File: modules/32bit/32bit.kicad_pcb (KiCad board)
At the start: 2 copper layers, 30.5 x 68.6 mm, 17 parts, among them J5 USB_C_Receptacle_USB2.0_14P, SW1 K2-1808SN-A4SW-01, SW2 K2-1808SN-A4SW-01, U1 ESP32-S3-WROOM-1U-N16R8

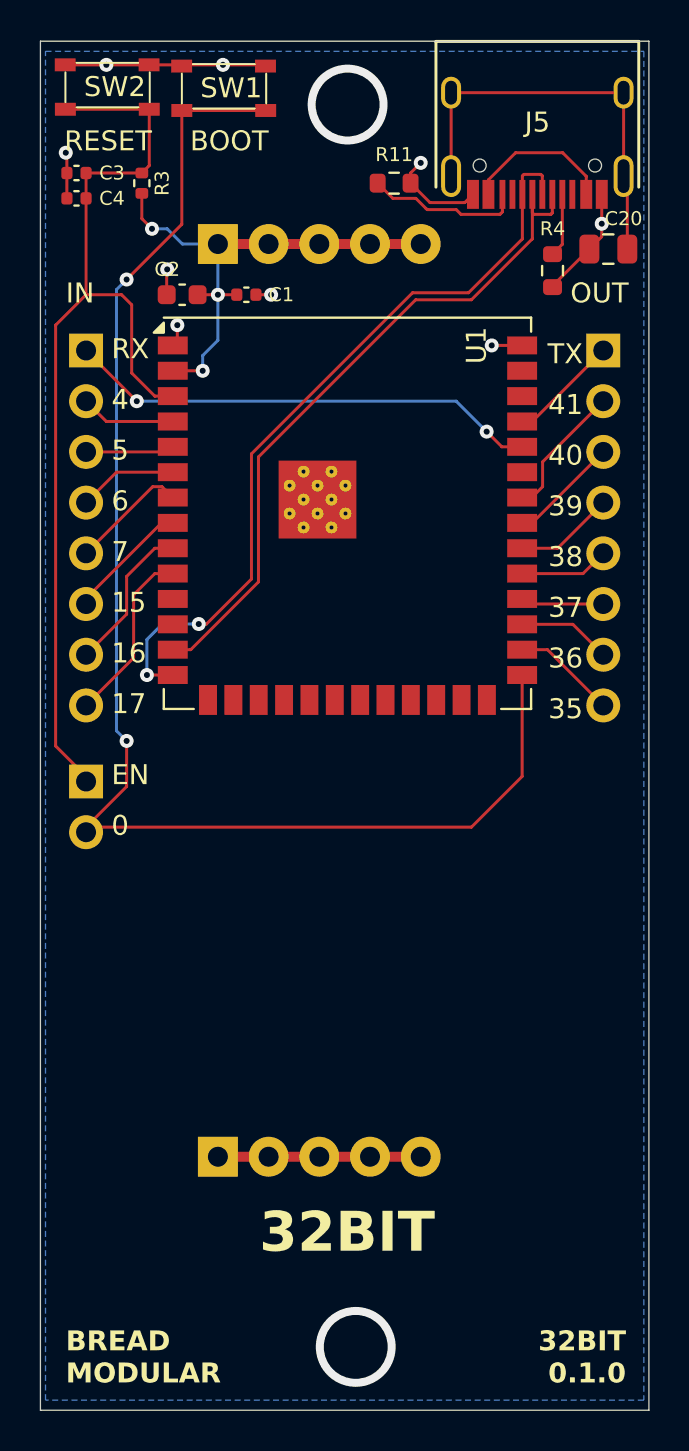
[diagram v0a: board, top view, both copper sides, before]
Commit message: Add 32bit schematics
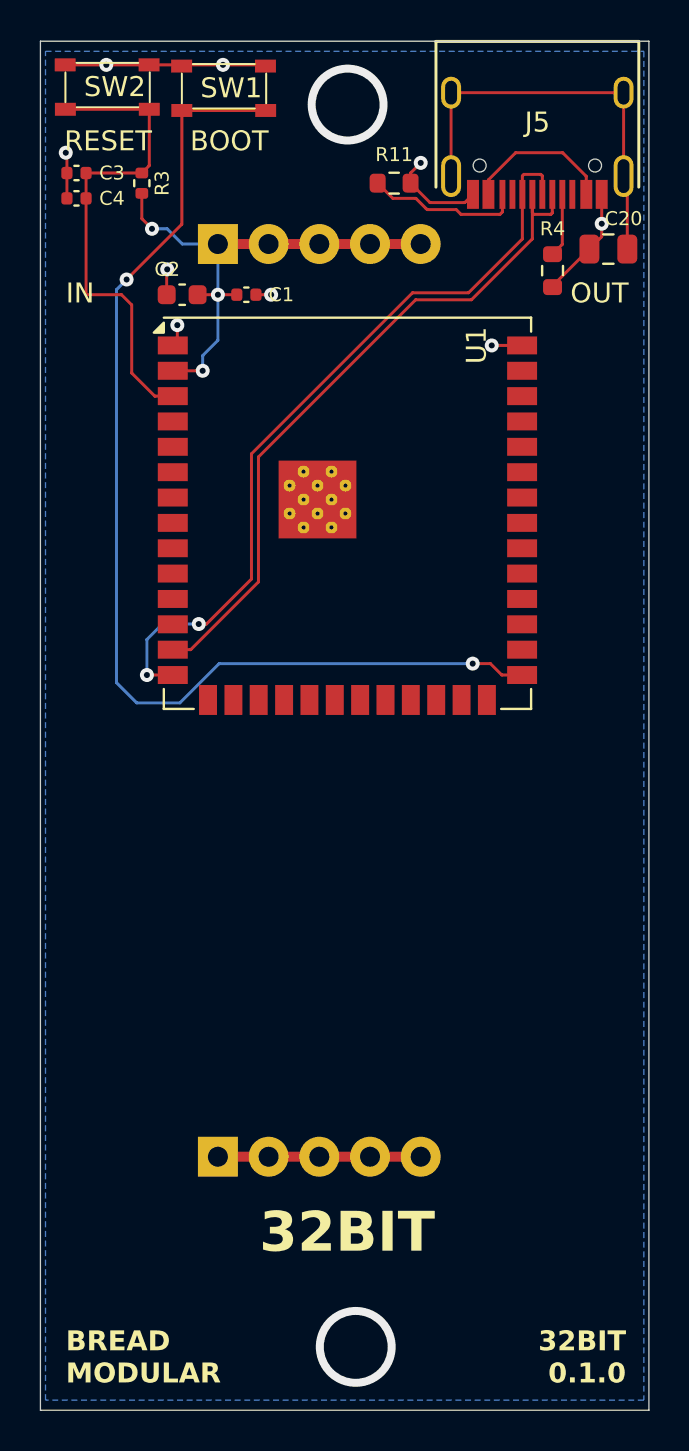
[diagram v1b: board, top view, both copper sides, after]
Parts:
- removed INPUT1, OUTPUT1: Conn_01x08_Socket, Connector_PinSocket_2.54mm:PinSocket_1x08_P2.54mm_Vertical
- removed INPUT2: Conn_01x02_Socket, Connector_PinSocket_2.54mm:PinSocket_1x02_P2.54mm_Vertical
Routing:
- net EN: track 50.3 -> 24.9 mm
- net RX: track 23.8 -> 0.00 mm, vias 2 -> 0
- net IO0: track 70.5 -> 56.0 mm
- net IO17: track 8.93 -> 0.00 mm
- net IO16: track 7.66 -> 0.00 mm
- net IO41: track 6.79 -> 0.00 mm
- net IO15: track 6.19 -> 0.00 mm
- net IO7: track 5.95 -> 0.00 mm
- net TX: track 5.54 -> 0.00 mm
- net IO40: track 5.54 -> 0.00 mm
- net IO35: track 5.22 -> 0.00 mm
- net IO39: track 5.01 -> 0.00 mm
- net IO6: track 4.98 -> 0.00 mm
- net IO4: track 4.76 -> 0.00 mm
- net IO36: track 4.70 -> 0.00 mm
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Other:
- board text removed: "0"
- board text removed: "15"
- board text removed: "16"
- board text removed: "17"
- board text removed: "35"
- board text removed: "36"
- board text removed: "37"
- board text removed: "38"
- board text removed: "39"
- board text removed: "4"
- board text removed: "40"
- board text removed: "41"
- board text removed: "5"
- board text removed: "6"
- board text removed: "7"
- board text removed: "EN"
- board text removed: "RX"
- board text removed: "TX"

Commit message: Finished basic routing
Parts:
- added C21: 0.1uf, Capacitor_SMD:C_0402_1005Metric, F.Cu at (67.3, 78.5)
- added C22: 0.1uf, Capacitor_SMD:C_0402_1005Metric, F.Cu at (65.8, 80.0)
- added C26: 0.1uf, Capacitor_SMD:C_0402_1005Metric, F.Cu at (73.4, 84.3)
- added C27: 10uf, Capacitor_SMD:C_0402_1005Metric, F.Cu at (64.8, 83.8)
- added C33: 10uf, Capacitor_SMD:C_0402_1005Metric, F.Cu at (73.4, 78.7)
- added C34: 0.1uf, Capacitor_SMD:C_0402_1005Metric, F.Cu at (73.4, 79.8)
- added C35: 10uf, Capacitor_SMD:C_0402_1005Metric, F.Cu at (73.4, 81.0)
- added C36: 0.1uf, Capacitor_SMD:C_0402_1005Metric, F.Cu at (73.3, 82.0)
- added C37: 10uf, Capacitor_SMD:C_0402_1005Metric, F.Cu at (73.4, 83.3)
- added C38: 10uf, Capacitor_SMD:C_0402_1005Metric, F.Cu at (73.3, 86.6)
- added C39: 0.1uf, Capacitor_SMD:C_0402_1005Metric, F.Cu at (73.4, 85.6)
- added C5: 10uf, Capacitor_SMD:C_0402_1005Metric, F.Cu at (66.3, 78.5)
- added C6: 0.1uf, Capacitor_SMD:C_0402_1005Metric, F.Cu at (54.9, 82.3)
- added D1: LED, LED_SMD:LED_0603_1608Metric, F.Cu at (55.2, 104.9)
- added INPUT1: Conn_01x05_Socket, Connector_PinSocket_2.54mm:PinSocket_1x05_P2.54mm_Vertical, B.Cu at (49.3, 56.4)
- added OUTPUT1: Conn_01x05_Socket, Connector_PinSocket_2.54mm:PinSocket_1x05_P2.54mm_Vertical, B.Cu at (75.2, 56.4)
- added R1: 1k, Resistor_SMD:R_0402_1005Metric, F.Cu at (75.2, 69.3)
- added R10: 100k, Resistor_SMD:R_0402_1005Metric, F.Cu at (49.8, 75.9)
- added R12: 100k, Resistor_SMD:R_0402_1005Metric, F.Cu at (50.0, 85.6)
- added R13: 1k, Resistor_SMD:R_0402_1005Metric, F.Cu at (65.3, 85.3)
- added R14: 33, Resistor_SMD:R_0402_1005Metric, F.Cu at (63.0, 75.7)
- added R17: 1k, Resistor_SMD:R_0402_1005Metric, F.Cu at (65.3, 86.4)
- added R18: 33, Resistor_SMD:R_0402_1005Metric, F.Cu at (64.3, 75.7)
- added R2: 1k, Resistor_SMD:R_0402_1005Metric, F.Cu at (75.2, 71.9)
- added R24: 4.7k, Resistor_SMD:R_0402_1005Metric, F.Cu at (71.6, 79.2)
- added R25: 4.7k, Resistor_SMD:R_0402_1005Metric, F.Cu at (69.8, 79.2)
- added R26: 33, Resistor_SMD:R_0402_1005Metric, F.Cu at (65.5, 75.7)
- added R5: 1.5k, Resistor_SMD:R_0402_1005Metric, F.Cu at (61.2, 100.3)
- added R6: 1.5k, Resistor_SMD:R_0402_1005Metric, F.Cu at (62.7, 100.3)
- added R7: 33, Resistor_SMD:R_0402_1005Metric, F.Cu at (60.5, 75.7)
- added R8: 33, Resistor_SMD:R_0402_1005Metric, F.Cu at (61.7, 75.7)
- added R9: 1k, Resistor_SMD:R_0402_1005Metric, F.Cu at (56.9, 104.4)
- added RV1: 50k, BreadModular_Pots:Potentiometer_RV09, F.Cu at (54.1, 93.0)
- added RV2: 50k, BreadModular_Pots:Potentiometer_RV09, F.Cu at (70.2, 93.0)
- added SW4: K2-1808SN-A4SW-01, BreadModular_MISC:K2-1808SN-A4SW-01, F.Cu at (51.2, 104.8)
- added U3: MCP6002-xSN, Package_SO:SOIC-8-1EP_3.9x4.9mm_P1.27mm_EP2.29x3mm, F.Cu at (51.6, 81.3)
- added U4: ~, Package_DFN_QFN:QFN-28-1EP_4x4mm_P0.45mm_EP2.4x2.4mm_ThermalVias, F.Cu at (68.6, 83.1)
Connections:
- net EN renamed Net-(SW2-B)
- net IO0 renamed Net-(SW1-B)
- net V_SUPPLY renamed +3V3
- U1 pad 10: IO17 -> unconnected-(U1-IO17-Pad10)
- U1 pad 11: unconnected-(U1-IO18-Pad11) -> LED_MODE
- U1 pad 12: unconnected-(U1-IO8-Pad12) -> BUTTON_MODE
- U1 pad 17: unconnected-(U1-IO9-Pad17) -> BUFF_CV1
- U1 pad 18: unconnected-(U1-IO10-Pad18) -> BUFF_CV2
- U1 pad 19: unconnected-(U1-IO11-Pad19) -> Net-(U1-IO11)
- U1 pad 20: unconnected-(U1-IO12-Pad20) -> Net-(U1-IO12)
- U1 pad 21: unconnected-(U1-IO13-Pad21) -> Net-(U1-IO13)
- U1 pad 22: unconnected-(U1-IO14-Pad22) -> Net-(U1-IO14)
- U1 pad 23: unconnected-(U1-IO21-Pad23) -> Net-(U1-IO21)
- U1 pad 24: unconnected-(U1-IO47-Pad24) -> CDATA
- U1 pad 25: unconnected-(U1-IO48-Pad25) -> CCLK
- U1 pad 28: IO35 -> unconnected-(U1-IO35-Pad28)
- U1 pad 29: IO36 -> unconnected-(U1-IO36-Pad29)
- U1 pad 30: IO37 -> unconnected-(U1-IO37-Pad30)
- U1 pad 31: IO38 -> unconnected-(U1-IO38-Pad31)
- U1 pad 32: IO39 -> unconnected-(U1-IO39-Pad32)
- U1 pad 33: IO40 -> unconnected-(U1-IO40-Pad33)
- U1 pad 34: IO41 -> unconnected-(U1-IO41-Pad34)
- U1 pad 38: unconnected-(U1-IO2-Pad38) -> Net-(U1-IO2)
- U1 pad 39: unconnected-(U1-IO1-Pad39) -> Net-(U1-IO1)
- U1 pad 4: IO4 -> unconnected-(U1-IO4-Pad4)
- U1 pad 5: IO5 -> unconnected-(U1-IO5-Pad5)
- U1 pad 6: IO6 -> unconnected-(U1-IO6-Pad6)
- U1 pad 7: IO7 -> unconnected-(U1-IO7-Pad7)
- U1 pad 8: IO15 -> unconnected-(U1-IO15-Pad8)
- U1 pad 9: IO16 -> unconnected-(U1-IO16-Pad9)
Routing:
- net +3V3: track 25.9 -> 131.0 mm, vias 3 -> 10
- net LED_MODE: track 0.00 -> 52.6 mm, vias 0 -> 2
- net Net-(SW1-B): track 56.0 -> 4.20 mm, vias 2 -> 0
- net AIN_1: track 0.00 -> 48.1 mm, vias 0 -> 1
- net BUTTON_MODE: track 0.00 -> 47.7 mm, vias 0 -> 2
- net AIN_2: track 0.00 -> 44.8 mm, vias 0 -> 1
- net RX: track 0.00 -> 42.6 mm, vias 0 -> 1
- net AOUT_1: track 0.00 -> 33.3 mm, vias 0 -> 1
- net Net-(U3A--): track 0.00 -> 31.3 mm
- net BUFF_CV2: track 0.00 -> 30.9 mm
- net Net-(U3B--): track 0.00 -> 29.3 mm, vias 0 -> 2
- net BUFF_CV1: track 0.00 -> 29.3 mm, vias 0 -> 2
- net AOUT_2: track 0.00 -> 29.3 mm, vias 0 -> 1
- net GND: track 37.8 -> 62.8 mm, vias 9 -> 23
- net CV2: track 0.00 -> 20.0 mm
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- added copper zone on In1.Cu, net GND
- removed copper zone on B.Cu, net GND
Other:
- copper layers 2 -> 4
- board text added: "MODE"

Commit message: Finished routing
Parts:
- moved R25 0.50 mm to (69.8, 78.7)
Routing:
- net Net-(SW1-B): track 4.20 -> 54.6 mm, vias 0 -> 2
- net +3V3: track 131.0 -> 135.2 mm
- net RX: track 42.6 -> 44.3 mm
- net GND: track 62.8 -> 63.4 mm
- net CDATA: track 9.49 -> 9.99 mm
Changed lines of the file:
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@@
 	(footprint "Resistor_SMD:R_0402_1005Metric"
 		(layer "F.Cu")
-		(at 69.85 79.246 90)
+		(at 69.85 78.742 90)
 		(descr "Resistor SMD 0402 (1005 Metric), square (rectangular) end terminal, IPC-7351 nominal, (Body size source: IPC-SM-782 page 72, https://www.pcb-3d.com/wordpress/wp-content/uploads/ipc-sm-782a_amendment_1_and_2.pdf), generated with kicad-footprint-generator")
 		(tags "resistor")
@@
 	)
 	(segment
-		(start 57.785 53.34)
-		(end 58.547 53.34)
-		(width 0.15)
-		(layer "F.Cu")
-		(net 1)
-	)
-	(segment
 		(start 53.314 52.096)
 		(end 53.34 52.07)
@@
 	)
 	(segment
+		(start 57.785 53.34)
+		(end 59.182 53.34)
+		(width 0.15)
+		(layer "F.Cu")
+		(net 1)
+	)
+	(segment
 		(start 50.292 41.826)
 		(end 48.232 41.826)
@@
 	)
 	(via
-		(at 58.547 53.34)
+		(at 59.182 53.34)
 		(size 0.7)
 		(drill 0.3)
@@
 	)
 	(segment
+		(start 69.85 78.232)
+		(end 69.85 77.216)
+		(width 0.15)
+		(layer "F.Cu")
+		(net 4)
+	)
+	(segment
 		(start 55.88 53.34)
 		(end 56.134 53.34)
@@
 		(net 4)
 	)
-	(segment
-		(start 69.85 78.736)
-		(end 69.85 77.978)
-		(width 0.15)
-		(layer "F.Cu")
-		(net 4)
-	)
 	(via
-		(at 69.85 77.978)
+		(at 69.85 77.216)
 		(size 0.5)
 		(drill 0.3)
@@
 	)
 	(segment
-		(start 66.548 74.676)
-		(end 69.85 77.978)
-		(width 0.5)
-		(layer "In2.Cu")
-		(net 4)
-	)
-	(segment
 		(start 72.39 77.216)
 		(end 71.628 77.978)
@@
 	)
 	(segment
+		(start 53.34 50.8)
+		(end 52.578 50.038)
+		(width 0.5)
+		(layer "In2.Cu")
+		(net 4)
+	)
+	(segment
 		(start 71.628 86.032)
 		(end 71.628 86.614)
@@
 	)
 	(segment
+		(start 70.866 77.216)
+		(end 71.628 77.978)
+		(width 0.15)
+		(layer "In2.Cu")
+		(net 4)
+	)
+	(segment
 		(start 50.292 80.01)
 		(end 54.356 84.074)
@@
 	)
 	(segment
-		(start 69.85 77.978)
-		(end 71.628 77.978)
+		(start 69.85 77.216)
+		(end 69.088 77.216)
+		(width 0.5)
+		(layer "In2.Cu")
+		(net 4)
+	)
+	(segment
+		(start 69.85 77.216)
+		(end 70.866 77.216)
 		(width 0.15)
 		(layer "In2.Cu")
@@
 	)
 	(segment
-		(start 69.088 77.978)
-		(end 67.31 79.756)
-		(width 0.15)
+		(start 66.548 74.676)
+		(end 49.276 74.676)
+		(width 0.5)
 		(layer "In2.Cu")
 		(net 4)
@@
 	)
 	(segment
+		(start 69.85 77.216)
+		(end 67.31 79.756)
+		(width 0.15)
+		(layer "In2.Cu")
+		(net 4)
+	)
+	(segment
 		(start 51.523 72.429)
 		(end 49.276 74.676)
@@
 	)
 	(segment
-		(start 69.85 77.978)
-		(end 69.088 77.978)
-		(width 0.15)
+		(start 55.88 50.8)
+		(end 53.34 50.8)
+		(width 0.5)
 		(layer "In2.Cu")
 		(net 4)
 	)
 	(segment
-		(start 49.276 74.676)
+		(start 69.088 77.216)
 		(end 66.548 74.676)
 		(width 0.5)
@@
 	)
 	(segment
-		(start 69.596 60.96)
-		(end 56.896 73.66)
+		(start 55.88 74.676)
+		(end 51.816 74.676)
 		(width 0.15)
 		(layer "B.Cu")
@@
 	)
 	(segment
-		(start 51.562 58.674)
-		(end 49.276 56.388)
+		(start 51.054 60.209611)
+		(end 51.054 58.166)
+		(width 0.15)
+		(layer "B.Cu")
+		(net 6)
+	)
+	(segment
+		(start 51.104 60.259612)
+		(end 51.054 60.209611)
+		(width 0.15)
+		(layer "B.Cu")
+		(net 6)
+	)
+	(segment
+		(start 69.596 60.96)
+		(end 55.88 74.676)
 		(width 0.15)
 		(layer "B.Cu")
@@
 	)
 	(segment
-		(start 56.896 73.66)
-		(end 52.324 73.66)
+		(start 51.104 73.964)
+		(end 51.104 60.259612)
 		(width 0.15)
 		(layer "B.Cu")
@@
 	)
 	(segment
-		(start 52.324 73.66)
-		(end 51.562 72.898)
+		(start 51.054 58.166)
+		(end 49.276 56.388)
 		(width 0.15)
 		(layer "B.Cu")
@@
 	)
 	(segment
-		(start 51.562 72.898)
-		(end 51.562 58.674)
+		(start 51.816 74.676)
+		(end 51.104 73.964)
 		(width 0.15)
 		(layer "B.Cu")
@@
 	)
 	(segment
-		(start 69.85 79.756)
-		(end 69.85 80.005812)
+		(start 69.041015 80.814797)
+		(end 69.041015 76.661015)
 		(width 0.15)
 		(layer "F.Cu")
@@
 	)
 	(segment
-		(start 69.85 80.005812)
-		(end 69.041015 80.814797)
+		(start 69.041015 80.060985)
+		(end 69.85 79.252)
 		(width 0.15)
 		(layer "F.Cu")
@@
 	(segment
 		(start 69.041015 80.814797)
-		(end 69.041015 76.661015)
+		(end 69.041015 80.060985)
 		(width 0.15)
 		(layer "F.Cu")
@@
 	)
 	(segment
+		(start 71.12 72.39)
+		(end 55.372 72.39)
+		(width 0.15)
+		(layer "F.Cu")
+		(net 51)
+	)
+	(segment
+		(start 54.102 44.14)
+		(end 54.074 44.112)
+		(width 0.15)
+		(layer "F.Cu")
+		(net 51)
+	)
+	(segment
 		(start 58.274 44.112)
 		(end 54.074 44.112)
@@
 		(net 51)
 	)
+	(segment
+		(start 54.102 45.466)
+		(end 54.102 44.14)
+		(width 0.15)
+		(layer "F.Cu")
+		(net 51)
+	)
+	(via
+		(at 55.372 72.39)
+		(size 0.5)
+		(drill 0.3)
+		(layers "F.Cu" "B.Cu")
+		(net 51)
+	)
+	(via
+		(at 54.102 45.466)
+		(size 0.5)
+		(drill 0.3)
+		(layers "F.Cu" "B.Cu")
+		(net 51)
+	)
+	(segment
+		(start 54.356 73.406)
+		(end 51.562 73.406)
+		(width 0.15)
+		(layer "B.Cu")
+		(net 51)
+	)
+	(segment
+		(start 51.455 73.299)
+		(end 51.455 72.39)
+		(width 0.15)
+		(layer "B.Cu")
+		(net 51)
+	)
+	(segment
+		(start 53.086 50.8)
+		(end 54.102 49.784)
+		(width 0.15)
+		(layer "B.Cu")
+		(net 51)
+	)
+	(segment
+		(start 54.102 49.784)
+		(end 54.102 45.466)
+		(width 0.15)
+		(layer "B.Cu")
+		(net 51)
+	)
+	(segment
+		(start 55.372 72.39)
+		(end 54.356 73.406)
+		(width 0.15)
+		(layer "B.Cu")
+		(net 51)
+	)
+	(segment
+		(start 51.455 72.39)
+		(end 51.455 52.431)
+		(width 0.15)
+		(layer "B.Cu")
+		(net 51)
+	)
+	(segment
+		(start 51.455 52.431)
+		(end 53.086 50.8)
+		(width 0.15)
+		(layer "B.Cu")
+		(net 51)
+	)
+	(segment
+		(start 51.562 73.406)
+		(end 51.455 73.299)
+		(width 0.15)
+		(layer "B.Cu")
+		(net 51)
+	)

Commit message: Add the production files
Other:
- board text added: "A1"
- board text added: "A2"
- board text added: "CV1"
- board text added: "CV2"
- board text added: "G1"
- board text added: "G2"
- board text added: "MDI"
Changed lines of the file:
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@@
 	)
 	(gr_text "IN"
-		(at 48.26 53.848 0)
-		(layer "F.SilkS")
-		(effects
-			(font
-				(size 1 1)
-				(thickness 0.15)
-			)
-			(justify left bottom)
+		(at 48.26 54.61 0)
+		(layer "F.SilkS" knockout)
+		(effects
+			(font
+				(size 1 1)
+				(thickness 0.15)
+			)
+			(justify left bottom)
+		)
+	)
+	(gr_text "CV2"
+		(at 73.66 100.838 0)
+		(layer "F.SilkS" knockout)
+		(effects
+			(font
+				(size 1 1)
+				(thickness 0.15)
+			)
+			(justify left bottom)
+		)
+	)
+	(gr_text "A1"
+		(at 74.422 59.69 0)
+		(layer "F.SilkS")
+		(effects
+			(font
+				(size 1 1)
+				(thickness 0.15)
+			)
+			(justify right bottom)
+		)
+	)
+	(gr_text "A1"
+		(at 50.165 59.69 0)
+		(layer "F.SilkS")
+		(effects
+			(font
+				(size 1 1)
+				(thickness 0.15)
+			)
+			(justify left bottom)
+		)
+	)
+	(gr_text "A2"
+		(at 74.422 62.23 0)
+		(layer "F.SilkS")
+		(effects
+			(font
+				(size 1 1)
+				(thickness 0.15)
+			)
+			(justify right bottom)
 		)
 	)
 	(gr_text "OUT"
-		(at 76.454 53.848 0)
-		(layer "F.SilkS")
-		(effects
-			(font
-				(size 1 1)
-				(thickness 0.15)
-			)
-			(justify right bottom)
+		(at 76.454 54.61 0)
+		(layer "F.SilkS" knockout)
+		(effects
+			(font
+				(size 1 1)
+				(thickness 0.15)
+			)
+			(justify right bottom)
+		)
+	)
+	(gr_text "MDI"
+		(at 74.422 57.15 0)
+		(layer "F.SilkS")
+		(effects
+			(font
+				(size 0.9 0.9)
+				(thickness 0.15)
+			)
+			(justify right bottom)
+		)
+	)
+	(gr_text "CV1"
+		(at 50.165 64.77 0)
+		(layer "F.SilkS")
+		(effects
+			(font
+				(size 0.9 0.9)
+				(thickness 0.15)
+			)
+			(justify left bottom)
+		)
+	)
+	(gr_text "CV1"
+		(at 47.498 100.838 0)
+		(layer "F.SilkS" knockout)
+		(effects
+			(font
+				(size 1 1)
+				(thickness 0.15)
+			)
+			(justify left bottom)
 		)
 	)
 	(gr_text "32BIT 0.1.0"
-		(at 76.2 104.775 0)
+		(at 76.2 104.648 0)
 		(layer "F.SilkS")
 		(effects
@@
 		)
 	)
+	(gr_text "MDI"
+		(at 50.165 57.15 0)
+		(layer "F.SilkS")
+		(effects
+			(font
+				(size 0.9 0.9)
+				(thickness 0.15)
+			)
+			(justify left bottom)
+		)
+	)
 	(gr_text "BOOT"
 		(at 58.42 46.228 0)
@@
 		)
 	)
+	(gr_text "G2"
+		(at 74.422 67.31 0)
+		(layer "F.SilkS")
+		(effects
+			(font
+				(size 1 1)
+				(thickness 0.15)
+			)
+			(justify right bottom)
+		)
+	)
+	(gr_text "G1"
+		(at 74.422 64.77 0)
+		(layer "F.SilkS")
+		(effects
+			(font
+				(size 1 1)
+				(thickness 0.15)
+			)
+			(justify right bottom)
+		)
+	)
+	(gr_text "A2"
+		(at 50.165 62.23 0)
+		(layer "F.SilkS")
+		(effects
+			(font
+				(size 1 1)
+				(thickness 0.15)
+			)
+			(justify left bottom)
+		)
+	)
+	(gr_text "CV2"
+		(at 50.165 67.31 0)
+		(layer "F.SilkS")
+		(effects
+			(font
+				(size 0.9 0.9)
+				(thickness 0.15)
+			)
+			(justify left bottom)
+		)
+	)

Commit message: 16bit: Moved CDATA & CCLK labels. They were just being marked wrongly in the ES8388 side
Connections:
- R24 pad 1: CCLK -> CDATA
- R25 pad 1: CDATA -> CCLK
- U1 pad 24: CDATA -> CCLK
- U1 pad 25: CCLK -> CDATA
- U4 pad 27: CCLK -> CDATA
- U4 pad 28: CDATA -> CCLK
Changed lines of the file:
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@@
 			(layers "F.Cu" "F.Mask" "F.Paste")
 			(roundrect_rratio 0.25)
-			(net 46 "CCLK")
+			(net 45 "CDATA")
 			(pinfunction "CDATA")
 			(pintype "input")
@@
 			(size 0.179289 0.179289)
 			(layers "F.Cu" "F.Mask" "F.Paste")
-			(net 45 "CDATA")
+			(net 46 "CCLK")
 			(pinfunction "CCLK")
 			(pintype "input")
@@
 			(layers "F.Cu" "F.Mask" "F.Paste")
 			(roundrect_rratio 0.25)
-			(net 45 "CDATA")
+			(net 46 "CCLK")
 			(pintype "passive")
 		)
@@
 			(size 1.5 0.9)
 			(layers "F.Cu" "F.Mask" "F.Paste")
-			(net 45 "CDATA")
+			(net 46 "CCLK")
 			(pinfunction "IO47")
 			(pintype "bidirectional")
@@
 			(size 1.5 0.9)
 			(layers "F.Cu" "F.Mask" "F.Paste")
-			(net 46 "CCLK")
+			(net 45 "CDATA")
 			(pinfunction "IO48")
 			(pintype "bidirectional")
@@
 			(layers "F.Cu" "F.Mask" "F.Paste")
 			(roundrect_rratio 0.25)
-			(net 46 "CCLK")
+			(net 45 "CDATA")
 			(pintype "passive")
 		)
@@
 	)
 	(segment
-		(start 66.815 74.435)
-		(end 66.815 73.64)
+		(start 71.628 79.756)
+		(end 70.736208 79.756)
 		(width 0.15)
 		(layer "F.Cu")
@@
 	)
 	(segment
-		(start 69.041015 80.814797)
-		(end 69.041015 76.661015)
+		(start 70.866 79.626208)
+		(end 70.866 77.321)
 		(width 0.15)
 		(layer "F.Cu")
@@
 	)
 	(segment
-		(start 69.041015 80.060985)
-		(end 69.85 79.252)
+		(start 70.547104 79.945104)
+		(end 70.866 79.626208)
 		(width 0.15)
 		(layer "F.Cu")
@@
 	)
 	(segment
-		(start 69.041015 80.814797)
-		(end 69.041015 80.060985)
+		(start 68.085 74.54)
+		(end 68.085 73.64)
 		(width 0.15)
 		(layer "F.Cu")
@@
 	)
 	(segment
-		(start 69.041015 76.661015)
-		(end 66.815 74.435)
+		(start 69.359213 81.132995)
+		(end 70.547104 79.945104)
 		(width 0.15)
 		(layer "F.Cu")
@@
 	)
 	(segment
-		(start 71.628 79.756)
-		(end 70.736208 79.756)
+		(start 70.736208 79.756)
+		(end 70.547104 79.945104)
 		(width 0.15)
 		(layer "F.Cu")
-		(net 46)
+		(net 45)
 	)
 	(segment
-		(start 70.866 79.626208)
-		(end 70.866 77.321)
+		(start 70.866 77.321)
+		(end 68.085 74.54)
 		(width 0.15)
 		(layer "F.Cu")
-		(net 46)
+		(net 45)
 	)
 	(segment
-		(start 70.547104 79.945104)
-		(end 70.866 79.626208)
+		(start 66.815 74.435)
+		(end 66.815 73.64)
 		(width 0.15)
 		(layer "F.Cu")
@@
 	)
 	(segment
-		(start 68.085 74.54)
-		(end 68.085 73.64)
+		(start 69.041015 80.814797)
+		(end 69.041015 76.661015)
 		(width 0.15)
 		(layer "F.Cu")
@@
 	)
 	(segment
-		(start 69.359213 81.132995)
-		(end 70.547104 79.945104)
+		(start 69.041015 80.060985)
+		(end 69.85 79.252)
 		(width 0.15)
 		(layer "F.Cu")
@@
 	)
 	(segment
-		(start 70.736208 79.756)
-		(end 70.547104 79.945104)
+		(start 69.041015 80.814797)
+		(end 69.041015 80.060985)
 		(width 0.15)
 		(layer "F.Cu")
@@
 	)
 	(segment
-		(start 70.866 77.321)
-		(end 68.085 74.54)
+		(start 69.041015 76.661015)
+		(end 66.815 74.435)
 		(width 0.15)
 		(layer "F.Cu")
